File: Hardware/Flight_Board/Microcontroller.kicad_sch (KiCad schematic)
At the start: 20 parts, among them J3 Conn_01x04, J4 Conn_01x06, SW1 SW_Push, U1 FT5HN

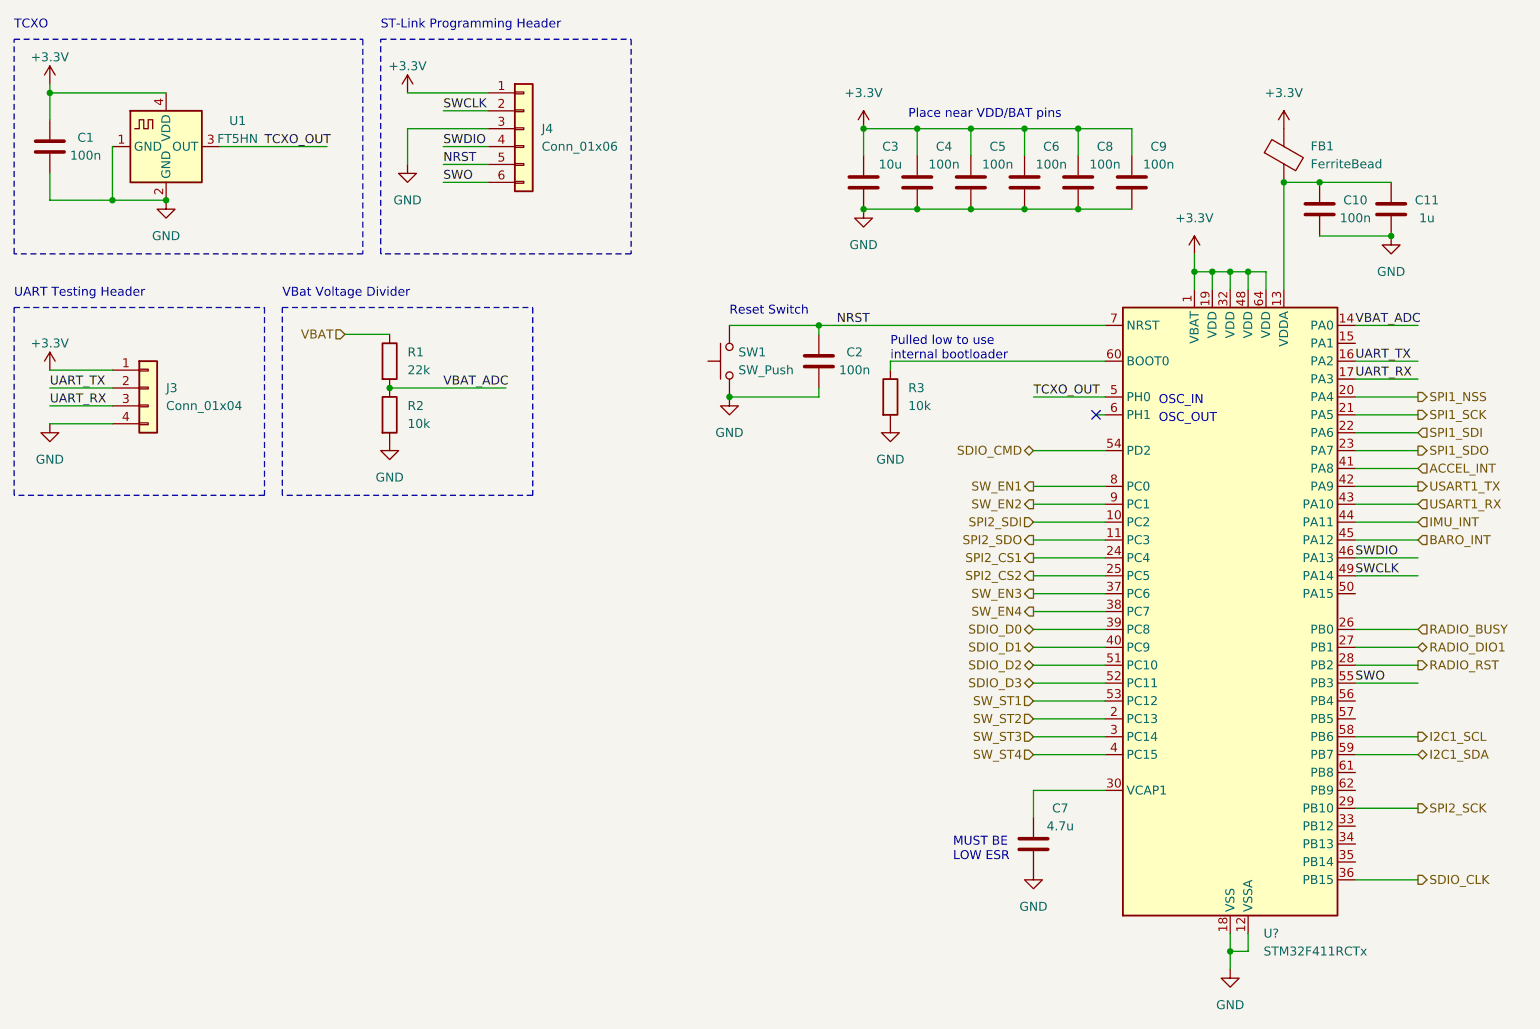
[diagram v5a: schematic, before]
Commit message: Add LEDs and test points
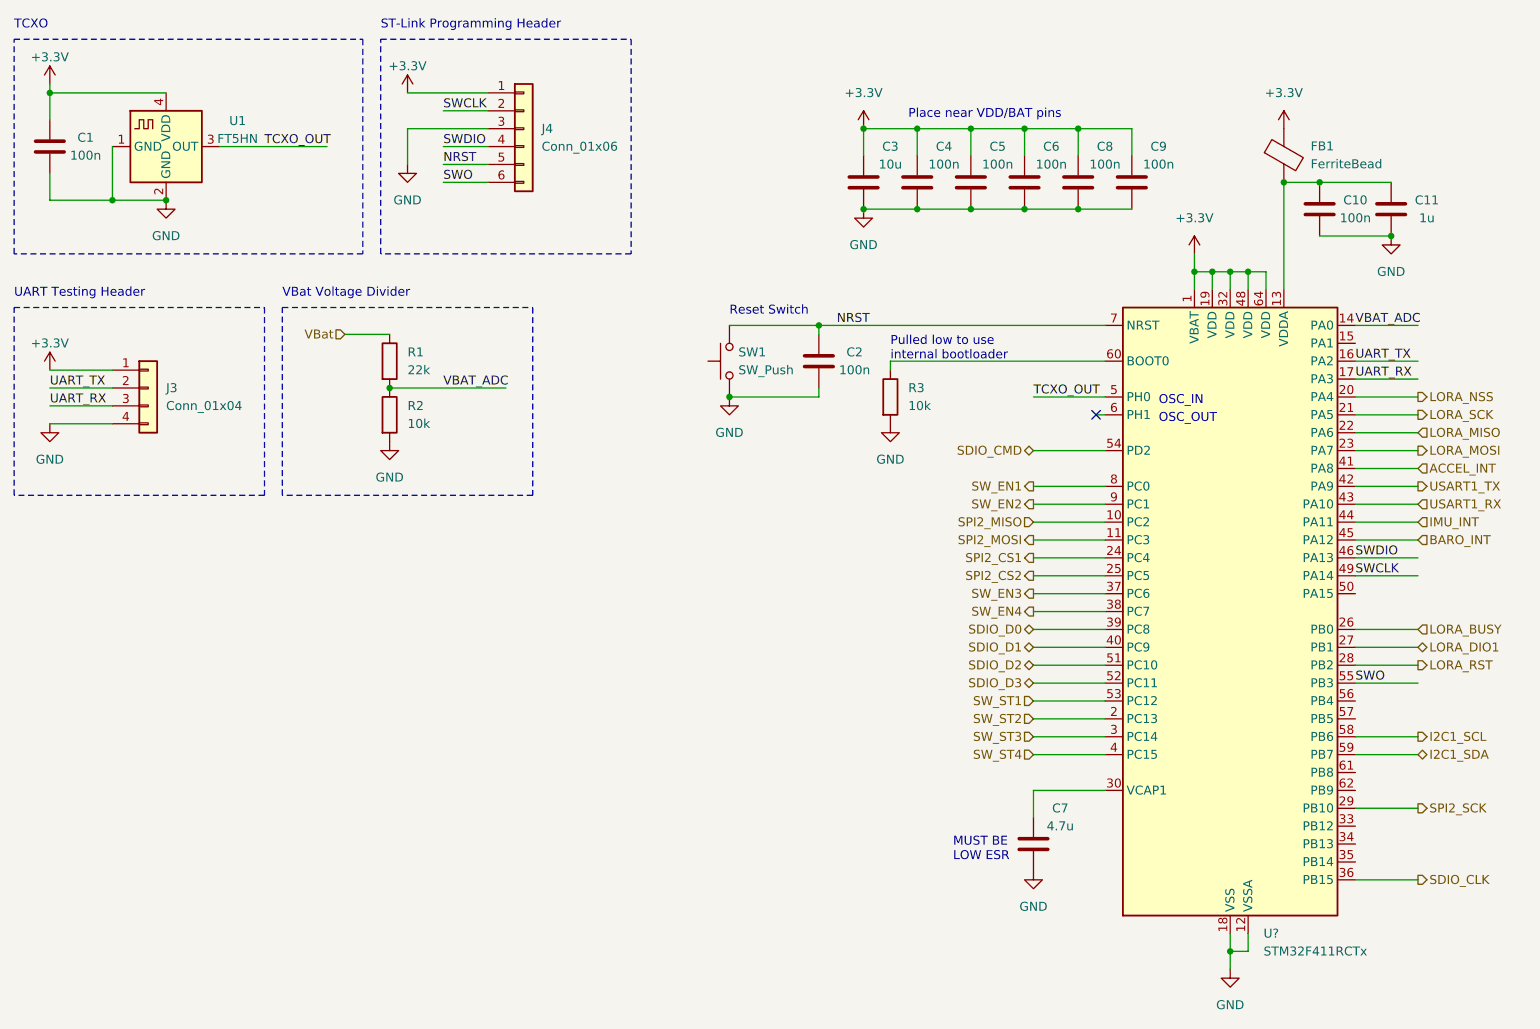
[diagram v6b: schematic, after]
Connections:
- net RADIO_BUSY renamed LORA_BUSY
- net RADIO_DIO1 renamed LORA_DIO1
- net RADIO_RST renamed LORA_RST
- net SPI1_NSS renamed LORA_NSS
- net SPI1_SCK renamed LORA_SCK
- net SPI1_SDI renamed LORA_MISO
- net SPI1_SDO renamed LORA_MOSI
- net SPI2_SDI renamed SPI2_MISO
- net SPI2_SDO renamed SPI2_MOSI
- net VBAT renamed VBat
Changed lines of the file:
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@@
     (effects (font (size 1.27 1.27)) (justify right))
   )
-  (hierarchical_label "SPI1_SDO" (shape output) (at 220.98 76.2 0) (fields_autoplaced)
+  (hierarchical_label "LORA_MOSI" (shape output) (at 220.98 76.2 0) (fields_autoplaced)
     (effects (font (size 1.27 1.27)) (justify left))
   )
-  (hierarchical_label "SPI1_SCK" (shape output) (at 220.98 71.12 0) (fields_autoplaced)
+  (hierarchical_label "LORA_SCK" (shape output) (at 220.98 71.12 0) (fields_autoplaced)
     (effects (font (size 1.27 1.27)) (justify left))
   )
-  (hierarchical_label "RADIO_RST" (shape output) (at 220.98 106.68 0) (fields_autoplaced)
+  (hierarchical_label "LORA_RST" (shape output) (at 220.98 106.68 0) (fields_autoplaced)
     (effects (font (size 1.27 1.27)) (justify left))
   )
@@
     (effects (font (size 1.27 1.27)) (justify right))
   )
-  (hierarchical_label "SPI2_SDI" (shape input) (at 166.37 86.36 180) (fields_autoplaced)
+  (hierarchical_label "SPI2_MISO" (shape input) (at 166.37 86.36 180) (fields_autoplaced)
     (effects (font (size 1.27 1.27)) (justify right))
   )
-  (hierarchical_label "RADIO_BUSY" (shape input) (at 220.98 101.6 0) (fields_autoplaced)
+  (hierarchical_label "LORA_BUSY" (shape input) (at 220.98 101.6 0) (fields_autoplaced)
     (effects (font (size 1.27 1.27)) (justify left))
   )
-  (hierarchical_label "SPI1_NSS" (shape output) (at 220.98 68.58 0) (fields_autoplaced)
+  (hierarchical_label "LORA_NSS" (shape output) (at 220.98 68.58 0) (fields_autoplaced)
     (effects (font (size 1.27 1.27)) (justify left))
   )
@@
     (effects (font (size 1.27 1.27)) (justify right))
   )
-  (hierarchical_label "SPI2_SDO" (shape output) (at 166.37 88.9 180) (fields_autoplaced)
+  (hierarchical_label "SPI2_MOSI" (shape output) (at 166.37 88.9 180) (fields_autoplaced)
     (effects (font (size 1.27 1.27)) (justify right))
   )
@@
     (effects (font (size 1.27 1.27)) (justify right))
   )
-  (hierarchical_label "SPI1_SDI" (shape input) (at 220.98 73.66 0) (fields_autoplaced)
+  (hierarchical_label "LORA_MISO" (shape input) (at 220.98 73.66 0) (fields_autoplaced)
     (effects (font (size 1.27 1.27)) (justify left))
   )
@@
     (effects (font (size 1.27 1.27)) (justify right))
   )
-  (hierarchical_label "VBAT" (shape input) (at 68.58 59.69 180) (fields_autoplaced)
+  (hierarchical_label "VBat" (shape input) (at 68.58 59.69 180) (fields_autoplaced)
     (effects (font (size 1.27 1.27)) (justify right))
   )
@@
     (effects (font (size 1.27 1.27)) (justify right))
   )
-  (hierarchical_label "RADIO_DIO1" (shape bidirectional) (at 220.98 104.14 0) (fields_autoplaced)
+  (hierarchical_label "LORA_DIO1" (shape bidirectional) (at 220.98 104.14 0) (fields_autoplaced)
     (effects (font (size 1.27 1.27)) (justify left))
   )

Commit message: final touches, bom, footprints
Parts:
- C1, C10, C11, C2, C3, C4, C5, C6, C8, C9: footprint (none) -> Capacitor_SMD:C_0603_1608Metric_Pad1.08x0.95mm_HandSolder
- C7: value 4.7u -> 4.7u LOWESR; footprint (none) -> Capacitor_SMD:C_0603_1608Metric_Pad1.08x0.95mm_HandSolder
- FB1, R1, R2, R3: footprint (none) -> Resistor_SMD:R_0603_1608Metric_Pad0.98x0.95mm_HandSolder
- J3: footprint (none) -> Connector_PinHeader_2.54mm:PinHeader_1x04_P2.54mm_Vertical
- J4: footprint (none) -> Connector_PinHeader_2.54mm:PinHeader_1x06_P2.54mm_Vertical
- SW1: footprint (none) -> Button_Switch_SMD:SW_SPST_PTS645
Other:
- note removed: "MUST BE LOW ESR"
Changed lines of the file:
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@@
-    (effects (font (size 1.27 1.27)) (justify left bottom))
-  )
-  (text "MUST BE\nLOW ESR" (at 154.94 134.62 0)
     (effects (font (size 1.27 1.27)) (justify left bottom))
   )
@@
       (effects (font (size 1.27 1.27)) (justify left))
     )
-    (property "Footprint" "" (at 144.272 68.58 90)
+    (property "Footprint" "Resistor_SMD:R_0603_1608Metric_Pad0.98x0.95mm_HandSolder" (at 144.272 68.58 90)
       (effects (font (size 1.27 1.27)) hide)
     )
@@
       (effects (font (size 1.27 1.27)) (justify left))
     )
-    (property "Footprint" "" (at 200.152 34.29 90)
+    (property "Footprint" "Resistor_SMD:R_0603_1608Metric_Pad0.98x0.95mm_HandSolder" (at 200.152 34.29 90)
       (effects (font (size 1.27 1.27)) hide)
     )
@@
       (effects (font (size 1.27 1.27)))
     )
-    (property "Footprint" "" (at 181.3052 41.91 0)
+    (property "Footprint" "Capacitor_SMD:C_0603_1608Metric_Pad1.08x0.95mm_HandSolder" (at 181.3052 41.91 0)
       (effects (font (size 1.27 1.27)) hide)
     )
@@
       (effects (font (size 1.27 1.27)) (justify right))
     )
-    (property "Footprint" "" (at 118.11 63.5 0)
+    (property "Footprint" "Button_Switch_SMD:SW_SPST_PTS645" (at 118.11 63.5 0)
       (effects (font (size 1.27 1.27)) hide)
     )
@@
       (effects (font (size 1.27 1.27)) (justify left))
     )
-    (property "Footprint" "" (at 73.152 63.5 90)
+    (property "Footprint" "Resistor_SMD:R_0603_1608Metric_Pad0.98x0.95mm_HandSolder" (at 73.152 63.5 90)
       (effects (font (size 1.27 1.27)) hide)
     )
@@
       (effects (font (size 1.27 1.27)))
     )
-    (property "Footprint" "" (at 27.6352 36.83 0)
+    (property "Footprint" "Capacitor_SMD:C_0603_1608Metric_Pad1.08x0.95mm_HandSolder" (at 27.6352 36.83 0)
       (effects (font (size 1.27 1.27)) hide)
     )
@@
       (effects (font (size 1.27 1.27)))
     )
-    (property "Footprint" "" (at 173.6852 41.91 0)
+    (property "Footprint" "Capacitor_SMD:C_0603_1608Metric_Pad1.08x0.95mm_HandSolder" (at 173.6852 41.91 0)
       (effects (font (size 1.27 1.27)) hide)
     )
@@
       (effects (font (size 1.27 1.27)))
     )
-    (property "Footprint" "" (at 150.8252 41.91 0)
+    (property "Footprint" "Capacitor_SMD:C_0603_1608Metric_Pad1.08x0.95mm_HandSolder" (at 150.8252 41.91 0)
       (effects (font (size 1.27 1.27)) hide)
     )
@@
       (effects (font (size 1.27 1.27)) (justify left))
     )
-    (property "Footprint" "" (at 73.152 71.12 90)
+    (property "Footprint" "Resistor_SMD:R_0603_1608Metric_Pad0.98x0.95mm_HandSolder" (at 73.152 71.12 90)
       (effects (font (size 1.27 1.27)) hide)
     )
@@
       (effects (font (size 1.27 1.27)))
     )
-    (property "Footprint" "" (at 218.1352 45.72 0)
+    (property "Footprint" "Capacitor_SMD:C_0603_1608Metric_Pad1.08x0.95mm_HandSolder" (at 218.1352 45.72 0)
       (effects (font (size 1.27 1.27)) hide)
     )
@@
       (effects (font (size 1.27 1.27)))
     )
-    (property "Value" "4.7u" (at 170.18 129.54 0)
-      (effects (font (size 1.27 1.27)))
-    )
-    (property "Footprint" "" (at 167.3352 135.89 0)
+    (property "Value" "4.7u LOWESR" (at 157.48 132.08 0)
+      (effects (font (size 1.27 1.27)))
+    )
+    (property "Footprint" "Capacitor_SMD:C_0603_1608Metric_Pad1.08x0.95mm_HandSolder" (at 167.3352 135.89 0)
       (effects (font (size 1.27 1.27)) hide)
     )
@@
       (effects (font (size 1.27 1.27)) (justify left))
     )
-    (property "Footprint" "" (at 40.64 67.31 0)
+    (property "Footprint" "Connector_PinHeader_2.54mm:PinHeader_1x04_P2.54mm_Vertical" (at 40.64 67.31 0)
       (effects (font (size 1.27 1.27)) hide)
     )
@@
       (effects (font (size 1.27 1.27)))
     )
-    (property "Footprint" "" (at 207.9752 45.72 0)
+    (property "Footprint" "Capacitor_SMD:C_0603_1608Metric_Pad1.08x0.95mm_HandSolder" (at 207.9752 45.72 0)
       (effects (font (size 1.27 1.27)) hide)
     )
@@
       (effects (font (size 1.27 1.27)) (justify left))
     )
-    (property "Footprint" "" (at 93.98 30.48 0)
+    (property "Footprint" "Connector_PinHeader_2.54mm:PinHeader_1x06_P2.54mm_Vertical" (at 93.98 30.48 0)
       (effects (font (size 1.27 1.27)) hide)
     )
@@
       (effects (font (size 1.27 1.27)))
     )
-    (property "Footprint" "" (at 166.0652 41.91 0)
+    (property "Footprint" "Capacitor_SMD:C_0603_1608Metric_Pad1.08x0.95mm_HandSolder" (at 166.0652 41.91 0)
       (effects (font (size 1.27 1.27)) hide)
     )
@@
       (effects (font (size 1.27 1.27)))
     )
-    (property "Footprint" "" (at 136.8552 67.31 0)
+    (property "Footprint" "Capacitor_SMD:C_0603_1608Metric_Pad1.08x0.95mm_HandSolder" (at 136.8552 67.31 0)
       (effects (font (size 1.27 1.27)) hide)
     )
@@
       (effects (font (size 1.27 1.27)))
     )
-    (property "Footprint" "" (at 143.2052 41.91 0)
+    (property "Footprint" "Capacitor_SMD:C_0603_1608Metric_Pad1.08x0.95mm_HandSolder" (at 143.2052 41.91 0)
       (effects (font (size 1.27 1.27)) hide)
     )
@@
       (effects (font (size 1.27 1.27)))
     )
-    (property "Footprint" "" (at 158.4452 41.91 0)
-      (effects (font (size 1.27 1.27)) hide)
-    )
+    (property "Footprint" "Capacitor_SMD:C_0603_1608Metric_Pad1.08x0.95mm_HandSolder" (at 158.4452 41.91 0)
+      (effects (font (size 1.27 1.27)) hide)
+    )

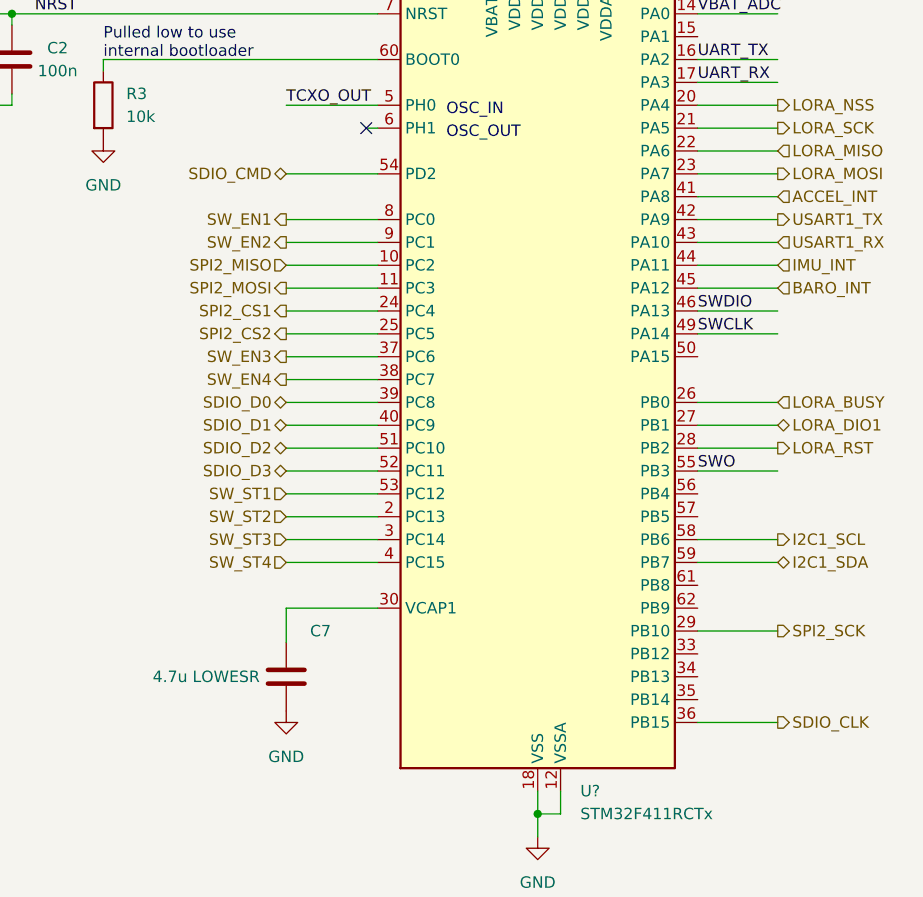
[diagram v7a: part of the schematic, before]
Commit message: flip mcu pins around, improve routability
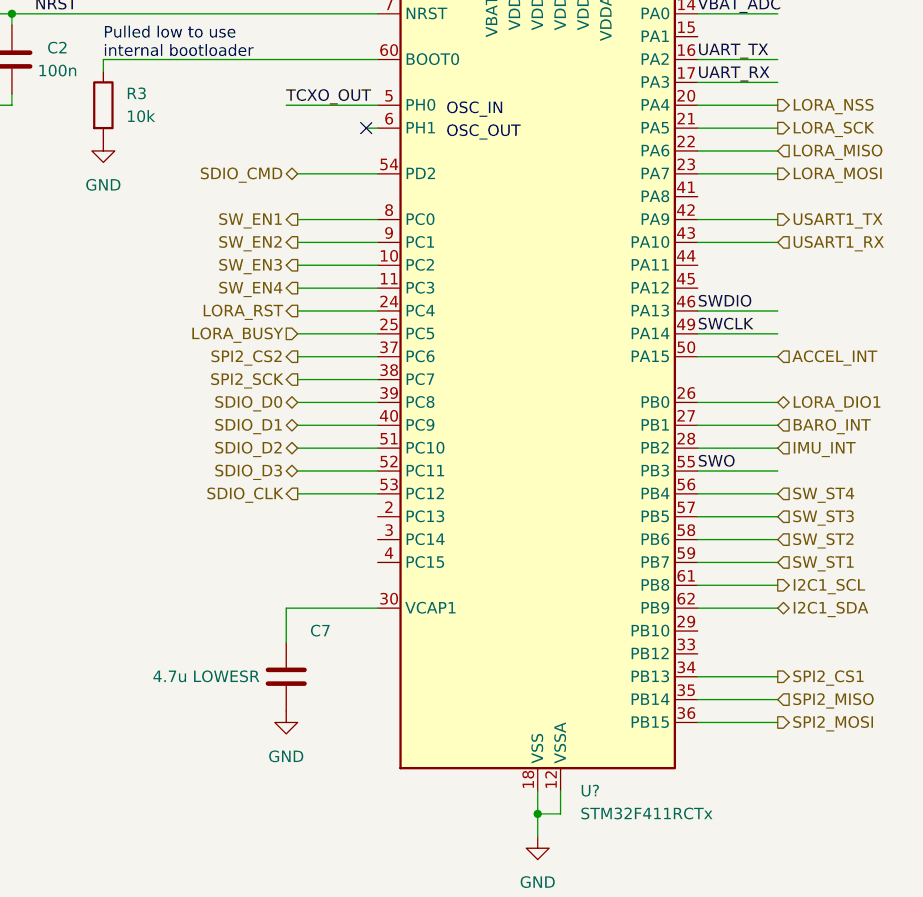
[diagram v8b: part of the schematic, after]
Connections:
- net ACCEL_INT: now also U?.50 (PA15); no longer U?.41 (PA8)
- net BARO_INT: now also U?.27 (PB1); no longer U?.45 (PA12)
- net I2C1_SCL: now also U?.61 (PB8); no longer U?.58 (PB6)
- net I2C1_SDA: now also U?.62 (PB9); no longer U?.59 (PB7)
- net IMU_INT: now also U?.28 (PB2); no longer U?.44 (PA11)
- net LORA_BUSY: now also U?.25 (PC5); no longer U?.26 (PB0)
- net LORA_DIO1: now also U?.26 (PB0); no longer U?.27 (PB1)
- net LORA_RST: now also U?.24 (PC4); no longer U?.28 (PB2)
- net SDIO_CLK: now also U?.53 (PC12); no longer U?.36 (PB15)
- net SPI2_CS1: now also U?.34 (PB13); no longer U?.24 (PC4)
- net SPI2_CS2: now also U?.37 (PC6); no longer U?.25 (PC5)
- net SPI2_MISO: now also U?.35 (PB14); no longer U?.10 (PC2)
- net SPI2_MOSI: now also U?.36 (PB15); no longer U?.11 (PC3)
- net SPI2_SCK: now also U?.38 (PC7); no longer U?.29 (PB10)
- net SW_EN3: now also U?.10 (PC2); no longer U?.37 (PC6)
- net SW_EN4: now also U?.11 (PC3); no longer U?.38 (PC7)
- net SW_ST1: now also U?.59 (PB7); no longer U?.53 (PC12)
- net SW_ST2: now also U?.58 (PB6); no longer U?.2 (PC13)
- net SW_ST3: now also U?.57 (PB5); no longer U?.3 (PC14)
- net SW_ST4: now also U?.56 (PB4); no longer U?.4 (PC15)
